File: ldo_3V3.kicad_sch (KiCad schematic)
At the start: 3 parts, among them U301 XC6220B331MR-G

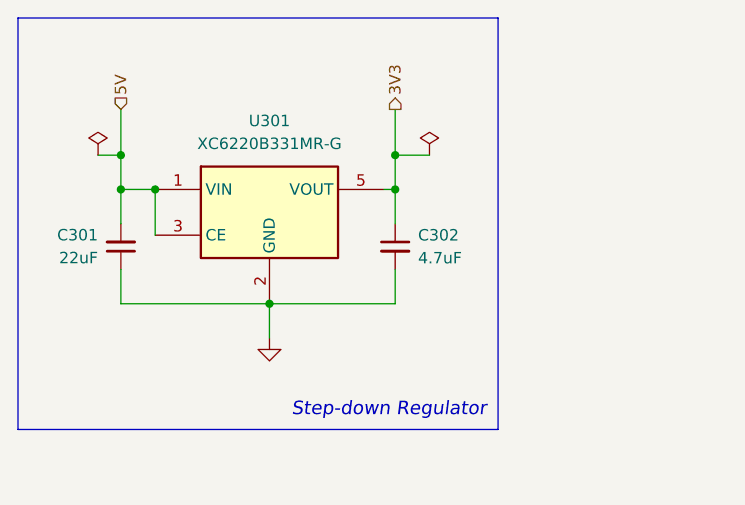
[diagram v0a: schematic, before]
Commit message: update schematic
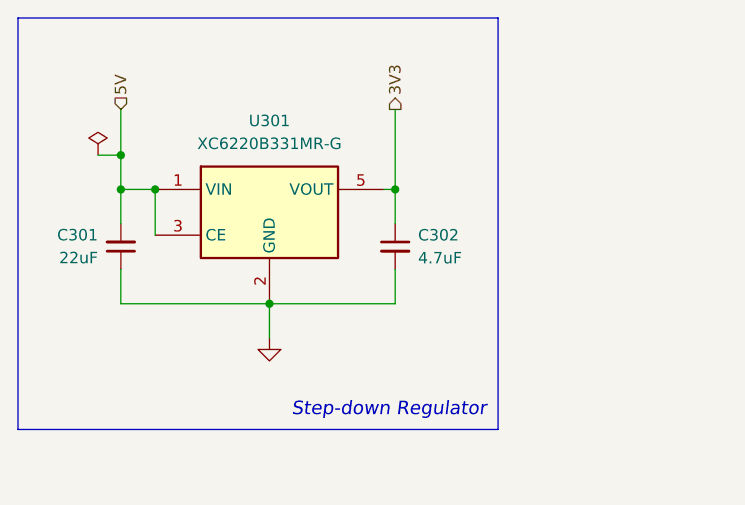
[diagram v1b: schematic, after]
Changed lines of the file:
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@@
   (junction (at 49.53 53.34) (diameter 0) (color 0 0 0 0)
-  )
-  (junction (at 76.2 49.53) (diameter 0) (color 0 0 0 0)
   )
   (junction (at 45.72 53.34) (diameter 0) (color 0 0 0 0)
@@
     (stroke (width 0) (type default))
   )
-  (wire (pts (xy 76.2 49.53) (xy 80.01 49.53))
-    (stroke (width 0) (type default))
-  )
   (polyline (pts (xy 34.29 34.29) (xy 34.29 80.01))
     (stroke (width 0) (type default))
@@
     (stroke (width 0) (type default))
   )
-  (wire (pts (xy 76.2 49.53) (xy 76.2 53.34))
-    (stroke (width 0) (type default))
-  )
   (polyline (pts (xy 34.29 34.29) (xy 87.63 34.29))
     (stroke (width 0) (type default))
   )
-  (wire (pts (xy 76.2 44.45) (xy 76.2 49.53))
+  (wire (pts (xy 76.2 44.45) (xy 76.2 53.34))
     (stroke (width 0) (type default))
   )
@@
     (property "Intersheetrefs" "${INTERSHEET_REFS}" (at 76.1206 38.5293 90)
       (effects (font (size 1.27 1.27)) (justify left) hide)
-    )
-  )
-  (symbol (lib_id "power:PWR_FLAG") (at 80.01 49.53 0) (unit 1)
-    (in_bom yes) (on_board yes) (dnp no) (fields_autoplaced)
-    (property "Reference" "#FLG0302" (at 80.01 47.625 0)
-      (effects (font (size 1.27 1.27)) hide)
-    )
-    (property "Value" "PWR_FLAG" (at 80.01 44.45 0)
-      (effects (font (size 1.27 1.27)) hide)
-    )
-    (property "Footprint" "" (at 80.01 49.53 0)
-      (effects (font (size 1.27 1.27)) hide)
-    )
-    (property "Datasheet" "~" (at 80.01 49.53 0)
-      (effects (font (size 1.27 1.27)) hide)
-    )
-    (pin "1")
-    (instances
-      (project "wled-esp32-control-board"
-        (path "/39949f26-7b4e-4f4c-975a-4ef261468b2a/d1f69b69-3231-4944-97e3-fdd35c90f911"
-          (reference "#FLG0302") (unit 1)
-        )
-      )
-      (project "iot_playground"
-        (path "/da21b043-c1be-47f1-86d6-d54e7594fd6d/b21a4c83-8caf-4c90-bfdc-6aae977d35b1"
-          (reference "#FLG0402") (unit 1)
-        )
-      )
     )
   )
@@
       (effects (font (size 1.27 1.27)) hide)
     )
-    (property "Datasheet" "https://datasheet.lcsc.com/lcsc/1810010324_Torex-Semicon-XC6220B331MR-G_C86534.pdf" (at 81.28 81.28 0)
+    (property "Datasheet" "https://www.torexsemi.com/file/xc6220/XC6220.pdf" (at 81.28 81.28 0)
       (effects (font (size 1.27 1.27)) hide)
     )

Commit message: add mouser part numbers
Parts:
- C301: Mouser (none) -> 581-06036D226MAT2A
- C302: Mouser (none) -> 581-0603ZD475KAT2A
- U301: Mouser (none) -> 865-XC6220B331MR-G
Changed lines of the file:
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@@
+      (effects (font (size 1.27 1.27)) hide)
+    )
+    (property "Mouser" "865-XC6220B331MR-G" (at 62.23 55.88 0)
       (effects (font (size 1.27 1.27)) hide)
     )
@@
       (effects (font (size 1.27 1.27)) hide)
     )
+    (property "Mouser" "581-06036D226MAT2A" (at 45.72 59.69 0)
+      (effects (font (size 1.27 1.27)) hide)
+    )
     (pin "1")
     (pin "2")
@@
       (effects (font (size 1.27 1.27)) hide)
     )
+    (property "Mouser" "581-0603ZD475KAT2A" (at 76.2 59.69 0)
+      (effects (font (size 1.27 1.27)) hide)
+    )

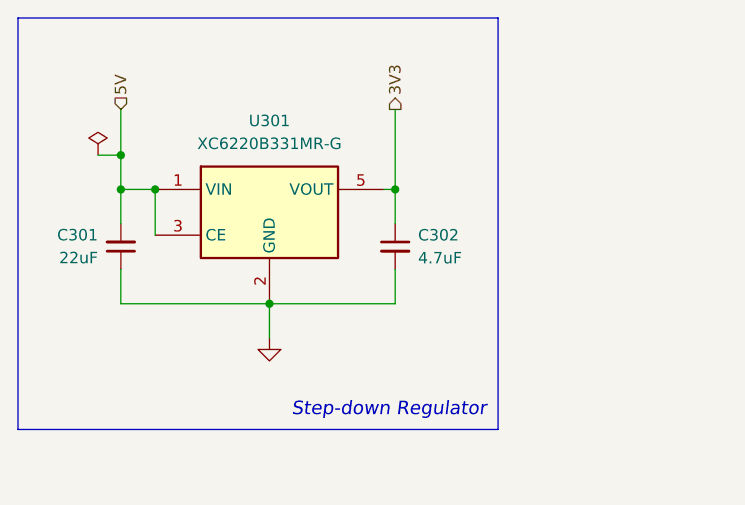
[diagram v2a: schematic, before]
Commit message: update design to replace CP2102 and LDO
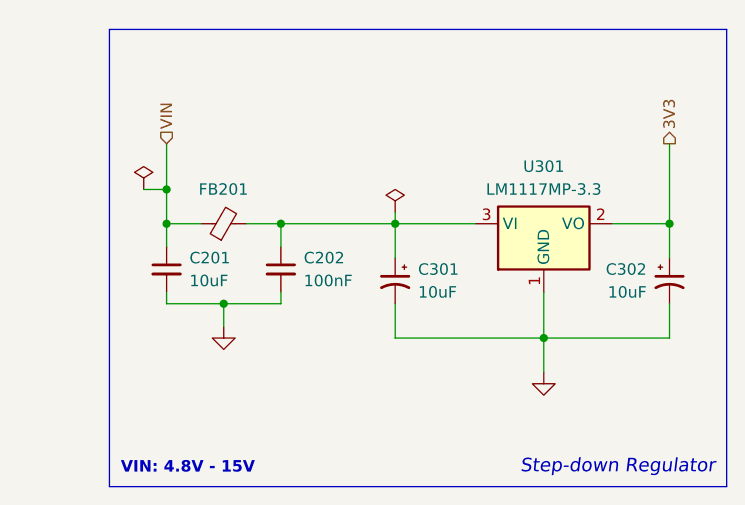
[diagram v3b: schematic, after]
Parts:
- removed C302: 4.7uF, Capacitor_SMD:C_0603_1608Metric, symbol Device:C_Small
- removed U301: XC6220B331MR-G, Package_TO_SOT_SMD:SOT-23-5, symbol Regulator_Linear:XC6220B331MR
- added C201: 10uF, Capacitor_SMD:C_0603_1608Metric, symbol Device:C_Small
- added C202: 100nF, Capacitor_SMD:C_0603_1608Metric, symbol Device:C_Small
- added C302: 10uF, Capacitor_Tantalum_SMD:CP_EIA-3216-10_Kemet-I, symbol Device:C_Polarized_Small_US
- added FB201: FerriteBead_Small, Resistor_SMD:R_0805_2012Metric, symbol Device:FerriteBead_Small
- added U301: LM1117MP-3.3, Package_TO_SOT_SMD:SOT-223-3_TabPin2, symbol Regulator_Linear:LM1117MP-3.3
- C301: value 22uF -> 10uF; footprint Capacitor_SMD:C_0603_1608Metric -> Capacitor_Tantalum_SMD:CP_EIA-3216-10_Kemet-I; symbol Device:C_Small -> Device:C_Polarized_Small_US; LCSC C59461 -> C185774; Mouser 581-06036D226MAT2A -> (none); Note (none) -> Tantalum
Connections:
- net 5V is gone; now on net GND: C301.2
- net 3V3: now also C302.1, U301.2 (VO)
- net GND: now also C201.2, C202.2, C302.2, U301.1 (GND); no longer C301.1
- new net: C202.1, C301.1, FB201.2, U301.3 (VI)
- new net VIN: C201.1, FB201.1
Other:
- note added: "VIN: 4.8V - 15V"

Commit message: update files to KiCad 8 format
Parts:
- renumbered C201 to C303, C202 to C304, FB201 to FB301
